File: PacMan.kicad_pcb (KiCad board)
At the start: 2 copper layers, 139.7 x 117.5 mm, 144 parts, among them J1 POWER+, J10 SEG2 CellMen, J11 SEG1 Balance, J12 SEG2 Balance, J13 AIR Left, J14 AIR Right, J15 SEG1, J16 SEG2, J2 POWER-, J3 TSV IN, J4 Charge Detection, J5 SEG1 CellMen, J6 BusBar Current Sensor, J7 Panel, J8 SLOOP, J9 GLV/CAN, K1 G5Q-1A4 DC24, K2 T9AS1D12-24, K3 T9AS1D12-24, Q1 BSS123, Q2 2N7002, Q3 BSS123, Q4 DMP10H4D2S, Q5 DMP10H4D2S, U1 MCP9804, U10 LTC4151, U11 INA592, U12 VIFSD1-S24-S5-SIP, U13 V7805-500, U14 Si8600AC, U15 Si8600AC, U16 TEC3-2419, U17 TEC3-2419, U18 AP2204K-5.0, U2 TEC2-4815WI, U3 ADM6320, U4 MCP2551-I-SN, U5 ESP32_TTGO_PSRAM, U6 MCP23008, U7 RTC, U8 ACHS-7122, U9 PDQE10-Q48-S24-D

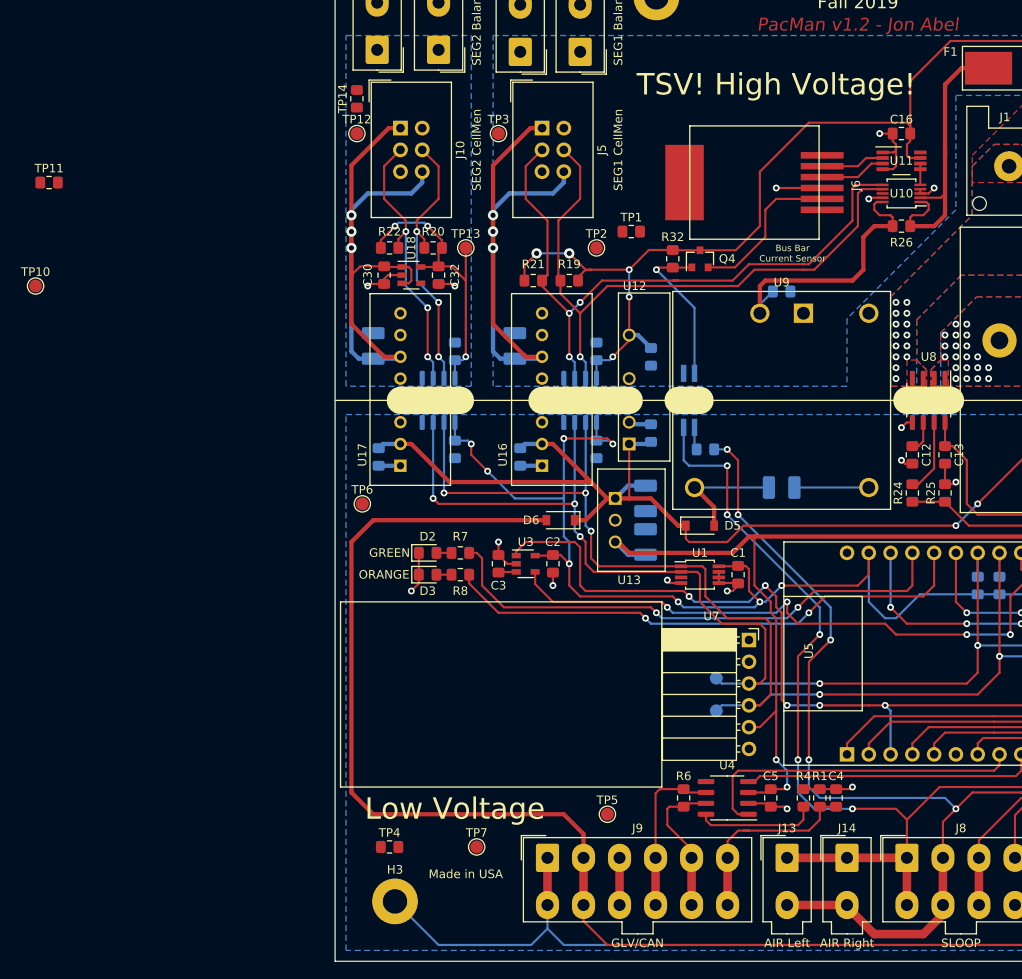
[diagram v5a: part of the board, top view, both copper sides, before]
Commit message: Started adding active charge measurement
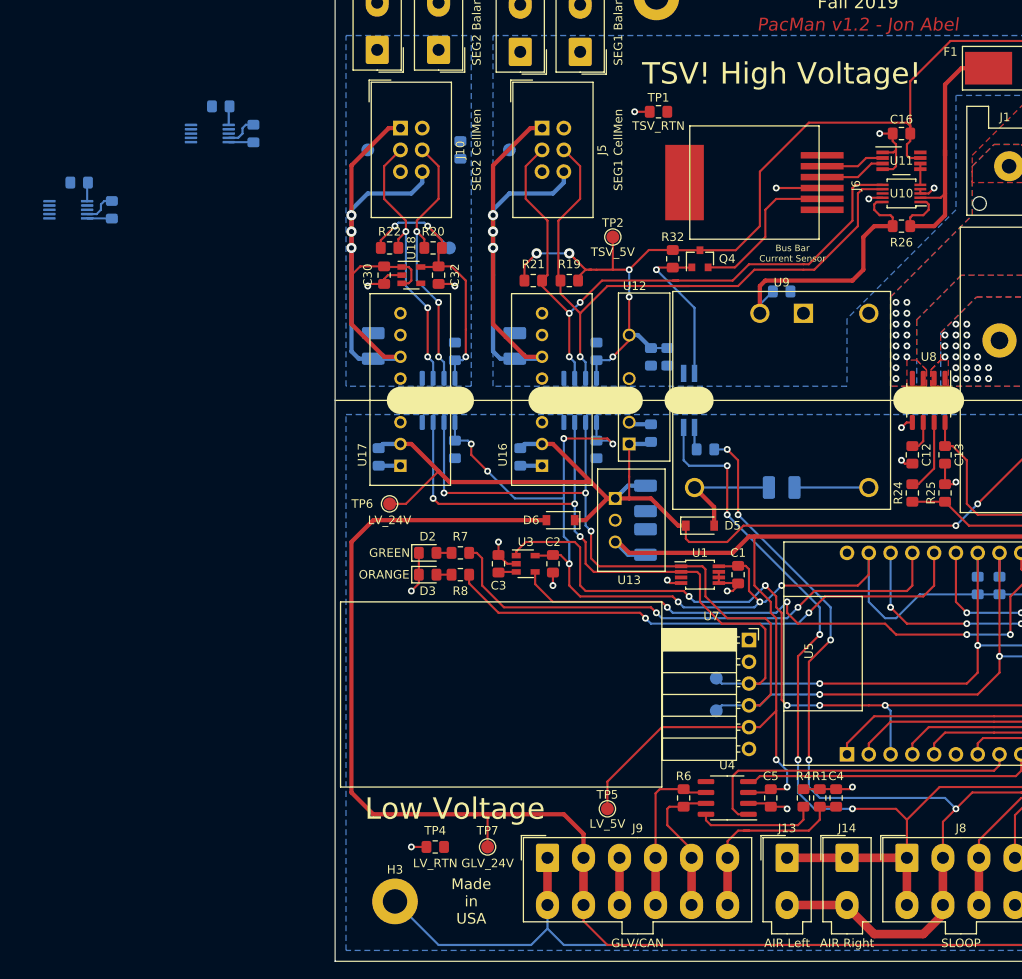
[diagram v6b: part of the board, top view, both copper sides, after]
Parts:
- removed TP10: SEG1_5V, TestPoint:TestPoint_Pad_D1.5mm
- removed TP11: SEG1_RTN, Resistor_SMD:R_0805_2012Metric_Pad1.15x1.40mm_HandSolder
- added C31: 0.1u/50V, Capacitor_SMD:C_0805_2012Metric_Pad1.15x1.40mm_HandSolder, B.Cu at (72.4, 54.6)
- added C33: 0.1u/50V, Capacitor_SMD:C_0805_2012Metric_Pad1.15x1.40mm_HandSolder, B.Cu at (55.9, 63.5)
- added R34: 500, Resistor_SMD:R_0805_2012Metric_Pad1.15x1.40mm_HandSolder, B.Cu at (124.5, 83.8)
- added R36: R, Resistor_SMD:R_0805_2012Metric_Pad1.15x1.40mm_HandSolder, B.Cu at (76.2, 57.8)
- added R37: R, Resistor_SMD:R_0805_2012Metric_Pad1.15x1.40mm_HandSolder, B.Cu at (59.7, 66.7)
- added U19: INA233, Package_SO:VSSOP-10_3x3mm_P0.5mm, B.Cu at (71.1, 57.8)
- added U20: INA233, Package_SO:VSSOP-10_3x3mm_P0.5mm, B.Cu at (54.6, 66.7)
- C28, C29: value 10u -> 10u/50V
- TP12, TP13, TP14, TP3: moved to B.Cu
- moved TP1 14.3 mm to (123.4, 55.2)
- moved TP14 13.5 mm to (100.3, 59.7), turned to 270 degrees
- moved TP4 5.33 mm to (97.4, 141.0)
- moved TP6 3.17 mm to (92.1, 101.0)
- moved TP2 2.29 mm to (118.1, 69.8)
- moved TP12 2.29 mm to (89.5, 59.7), turned to 270 degrees
- moved TP3 2.29 mm to (106.0, 59.7), turned to 270 degrees
- moved TP13 1.91 mm to (99.1, 71.1), turned to 270 degrees
- moved TP7 1.27 mm to (103.5, 141.0)
- moved TP5 0.63 mm to (117.5, 136.5)
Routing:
- net /LV_5V: track 134.8 -> 157.1 mm
- net /LV_24V: track 188.1 -> 195.4 mm
- net /SEG1_5V: track 186.0 -> 191.7 mm
- net /SEG2_9V: track 76.9 -> 81.8 mm
- net /SEG1_9V: track 66.8 -> 71.7 mm
- net /Charging/SEG1+: track 0.00 -> 3.88 mm
- net /Charging/SEG2+: track 0.00 -> 3.88 mm
- net /GLV_24V: track 175.5 -> 179.3 mm
- net /Charging/BAL_SEG1+: track 0.00 -> 2.89 mm
- net /Charging/BAL_SEG2+: track 0.00 -> 2.89 mm
- net /Charging/SEG1_5V: track 0.00 -> 2.21 mm
- net /Charging/SEG2_5V: track 0.00 -> 2.21 mm
- net /GLV_RTN: track 83.6 -> 85.4 mm, vias 19 -> 20
- net /PACK_RTN: track 29.7 -> 31.4 mm, vias 21 -> 22

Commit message: Schematic work, placed some components on the PCB
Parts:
- removed Q3: BSS123, Package_TO_SOT_SMD:SOT-23
- added BT1: BR1225, Battery:BatteryHolder_Keystone_103_1x20mm, F.Cu at (-19.1, 162.9)
- added C34: 1u/50V, Capacitor_SMD:C_0805_2012Metric_Pad1.15x1.40mm_HandSolder, F.Cu at (0.14, 176.7)
- added D7: LED_CHRG, LED_SMD:LED_0805_2012Metric_Pad1.15x1.40mm_HandSolder, F.Cu at (37.4, 152.2)
- added R41: R, Resistor_SMD:R_0805_2012Metric_Pad1.15x1.40mm_HandSolder, F.Cu at (37.4, 155.1)
- added Y1: RTC_32K, Crystal:Crystal_SMD_SeikoEpson_MC405-2Pin_9.6x4.1mm_HandSoldering, F.Cu at (-12.2, 178.0)
- Q2: value 2N7002 -> DMN3730U
- U7: value RTC -> BQ32002; footprint Connector_PinSocket_2.54mm:PinSocket_1x06_P2.54mm_Horizontal -> Package_SO:SOIC-8_3.9x4.9mm_P1.27mm
- moved Q2 175.2 mm to (42.0, 152.9)
- moved U7 126.9 mm to (12.6, 153.9)
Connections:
- C31 pad 1: /Charging/SEG1_RTN -> /PACK_RTN
- C31 pad 2: /Charging/SEG1_5V -> /SEG1_5V
- C33 pad 1: /Charging/SEG2_RTN -> /SEG2_RTN
- C33 pad 2: /Charging/SEG2_5V -> /SEG2_5V
- D4 pad 2: Net-(D4-Pad2) -> /CHRG_LED
- K2 pad 2: Net-(D4-Pad2) -> /CHRG_LED
- K3 pad 2: Net-(D4-Pad2) -> /CHRG_LED
- Q2 pad 3: Net-(D4-Pad2) -> /CHRG_LED
- U19 pad 1: /Charging/SEG1_RTN -> /PACK_RTN
- U19 pad 2: /Charging/SEG1_RTN -> /PACK_RTN
- U19 pad 4: (no net) -> /SDA_SEG1
- U19 pad 5: (no net) -> /SCL_SEG1
- U19 pad 6: /Charging/SEG1_5V -> /SEG1_5V
- U19 pad 7: /Charging/SEG1_RTN -> /PACK_RTN
- U20 pad 1: /Charging/SEG2_RTN -> /SEG2_RTN
- U20 pad 2: /Charging/SEG2_RTN -> /SEG2_RTN
- U20 pad 4: (no net) -> /SDA_SEG2
- U20 pad 5: (no net) -> /SCL_SEG2
- U20 pad 6: /Charging/SEG2_5V -> /SEG2_5V
- U20 pad 7: /Charging/SEG2_RTN -> /SEG2_RTN
- U7 pad 1: (no net) -> Net-(U7-Pad1)
- U7 pad 2: (no net) -> Net-(U7-Pad2)
- U7 pad 3: /SCL_GLV -> Net-(BT1-Pad1)
- U7 pad 4: /SDA_GLV -> /GLV_RTN
- U7 pad 5: /LV_5V -> /SDA_GLV
- U7 pad 6: /GLV_RTN -> /SCL_GLV
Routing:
- net /CHRG_LED: track 19.7 -> 68.7 mm
- net Net-(D4-Pad2): track 49.0 -> 0.00 mm
- net /PACK_FUSED: track 34.7 -> 21.3 mm
- net /SEG1_5V: track 191.7 -> 182.5 mm
- net /PACK_RTN: track 31.4 -> 24.2 mm
- net /Charging/SEG1_5V: track 2.21 -> 0.00 mm
- net /SEG2_5V: track 34.9 -> 37.1 mm
- net /Charging/SEG2_5V: track 2.21 -> 0.00 mm
- net /Power/DCHRG_CURRENT: track 2.46 -> 1.81 mm

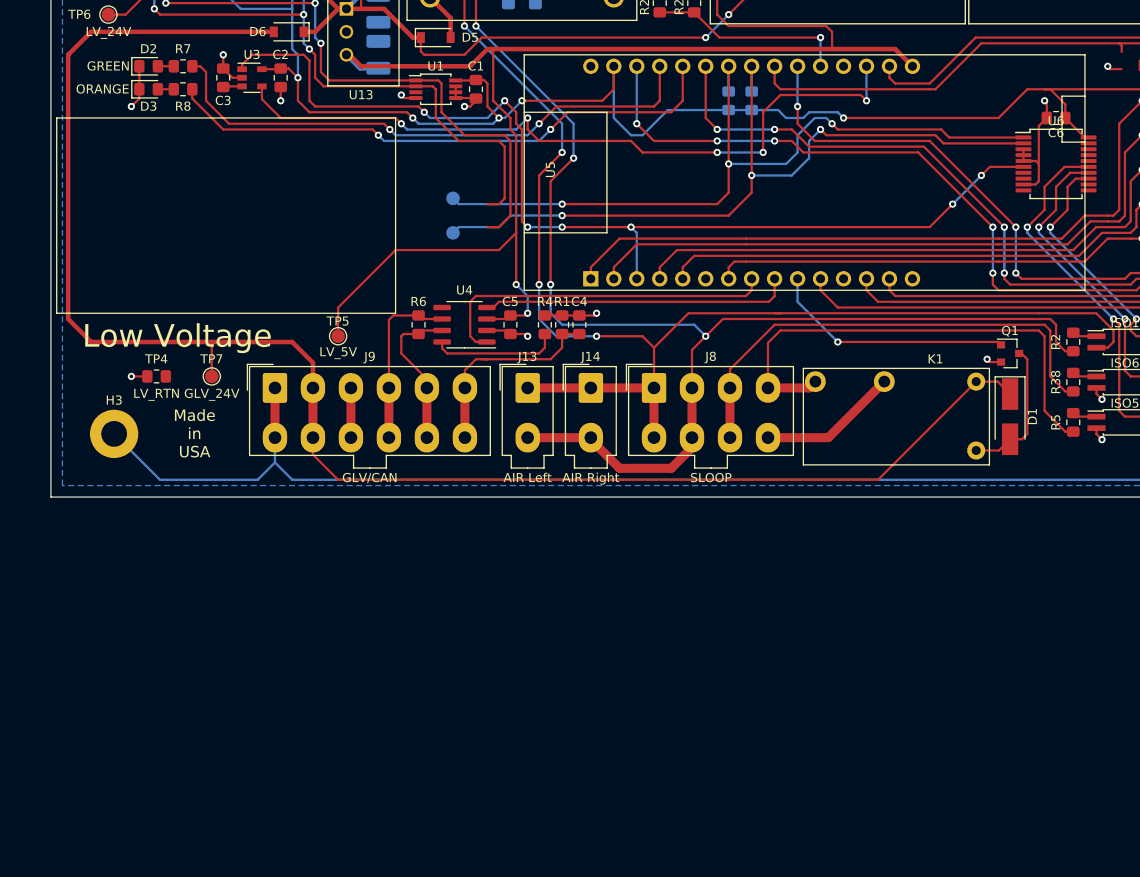
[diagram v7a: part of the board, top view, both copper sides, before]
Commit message: started moving over to new esp dev kit
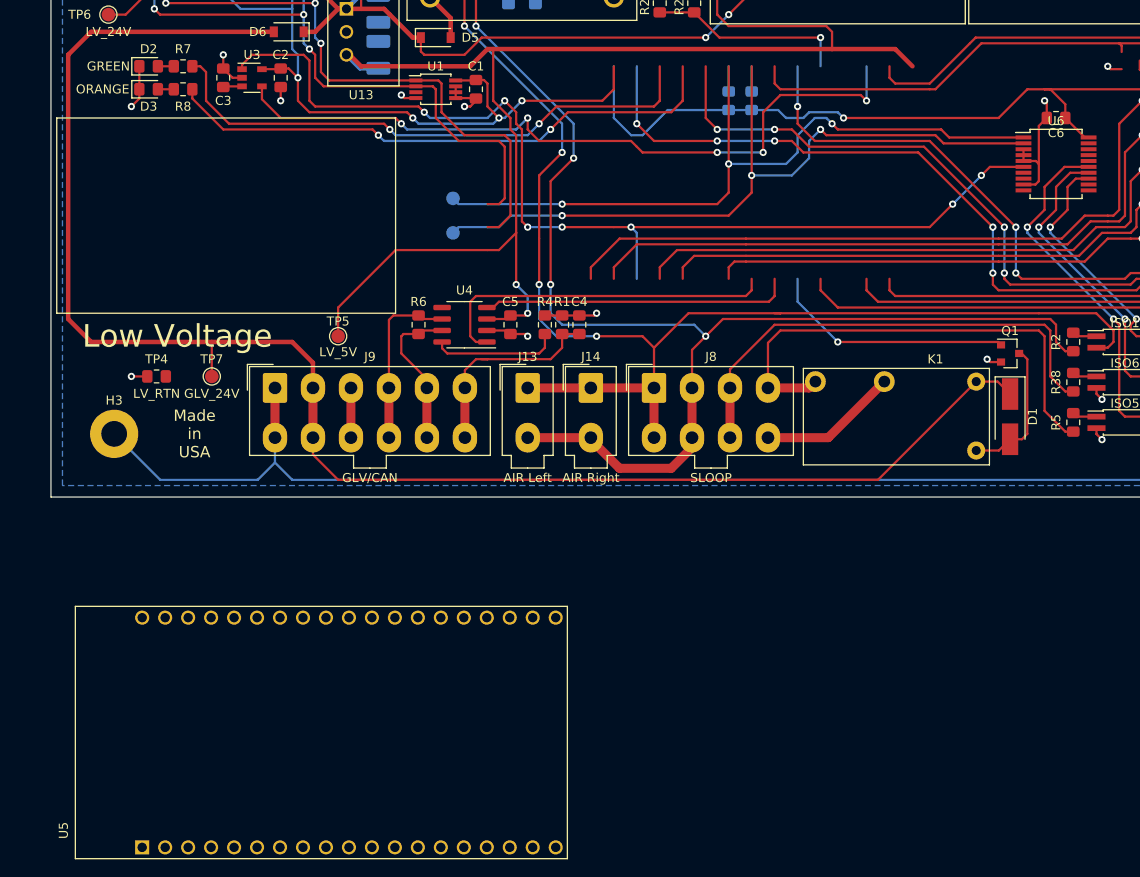
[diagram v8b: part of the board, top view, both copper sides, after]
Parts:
- U5: value ESP32_TTGO_PSRAM -> ESP32_DEVKITC; footprint Lafayette_Electric_Car_Footprints:ESP32TTGOT8 -> Lafayette_Electric_Car_Footprints:MODULE_ESP32-DEVKITC-32D
- moved U5 58.4 mm to (115.6, 180.3)
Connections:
- U5 pad 1: /MCU/BTN_LEFT_MCU -> /LV_3V3
- U5 pad 10: /MCU/SLOOP_EN -> /MCU/CANRX
- U5 pad 11: /DISP_CLK -> /MCU/SLOOP_EN
- U5 pad 12: (no net) -> /DISP_CLK
- U5 pad 13: /DISP_DIN -> (no net)
- U5 pad 14: /DISP_CS -> /GLV_RTN
- U5 pad 15: /GLV_RTN -> /DISP_DIN
- U5 pad 16: /LV_5V -> (no net)
- U5 pad 17: /~CHRG_DETECT -> (no net)
- U5 pad 18: /MCU/WATCHDOG -> (no net)
- U5 pad 19: /GLV_RTN -> /LV_5V
- U5 pad 2: /MCU/BTN_RIGHT_MCU -> /MCU/~RESET
- U5 pad 20: /CHRG_CURRENT -> /GLV_RTN
- U5 pad 21: /DISP_BUSY -> (no net)
- U5 pad 22: /CHRG_EN -> /DISP_DC
- U5 pad 25: /DISP_DC -> /DISP_RST
- U5 pad 26: /MCU/LED2 -> /GLV_RTN
- U5 pad 28: /DISP_RST -> /MCU/LED2
- U5 pad 29: /LV_3V3 -> /DISP_BUSY
- U5 pad 3: /MCU/~RESET -> /MCU/BTN_CENTER_MCU
- U5 pad 30: /GLV_RTN -> /~CHRG_DETECT
- U5 pad 6: (no net) -> /MCU/BTN_LEFT_MCU
- U5 pad 7: /MCU/BTN_CENTER_MCU -> /MCU/BTN_RIGHT_MCU
- U5 pad 8: /MCU/CANTX -> (no net)
- U5 pad 9: /MCU/CANRX -> /MCU/CANTX
